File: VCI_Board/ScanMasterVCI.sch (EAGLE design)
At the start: 74 parts, among them IC1 XMEGA16A4A, IC2 CD4081B, IC4 SN74AHCT1G04, IC6 TL331, IC7 74AHCT1G32DBV, IC8 SN74AHCT1G04, Q1 MMBT3904, Q2 MMBT4403LT1SMD, Q3 MMBT4403, Q4 MMBT3904, Q6 NC7SZ18, Q7 ZXMP6A17G, Q9 NC7SZ18, U1 MAX17502FATB+, U2 SN65HVDA195-Q1, U3 MAX17502EATB+, U4 MAX13444EASA+

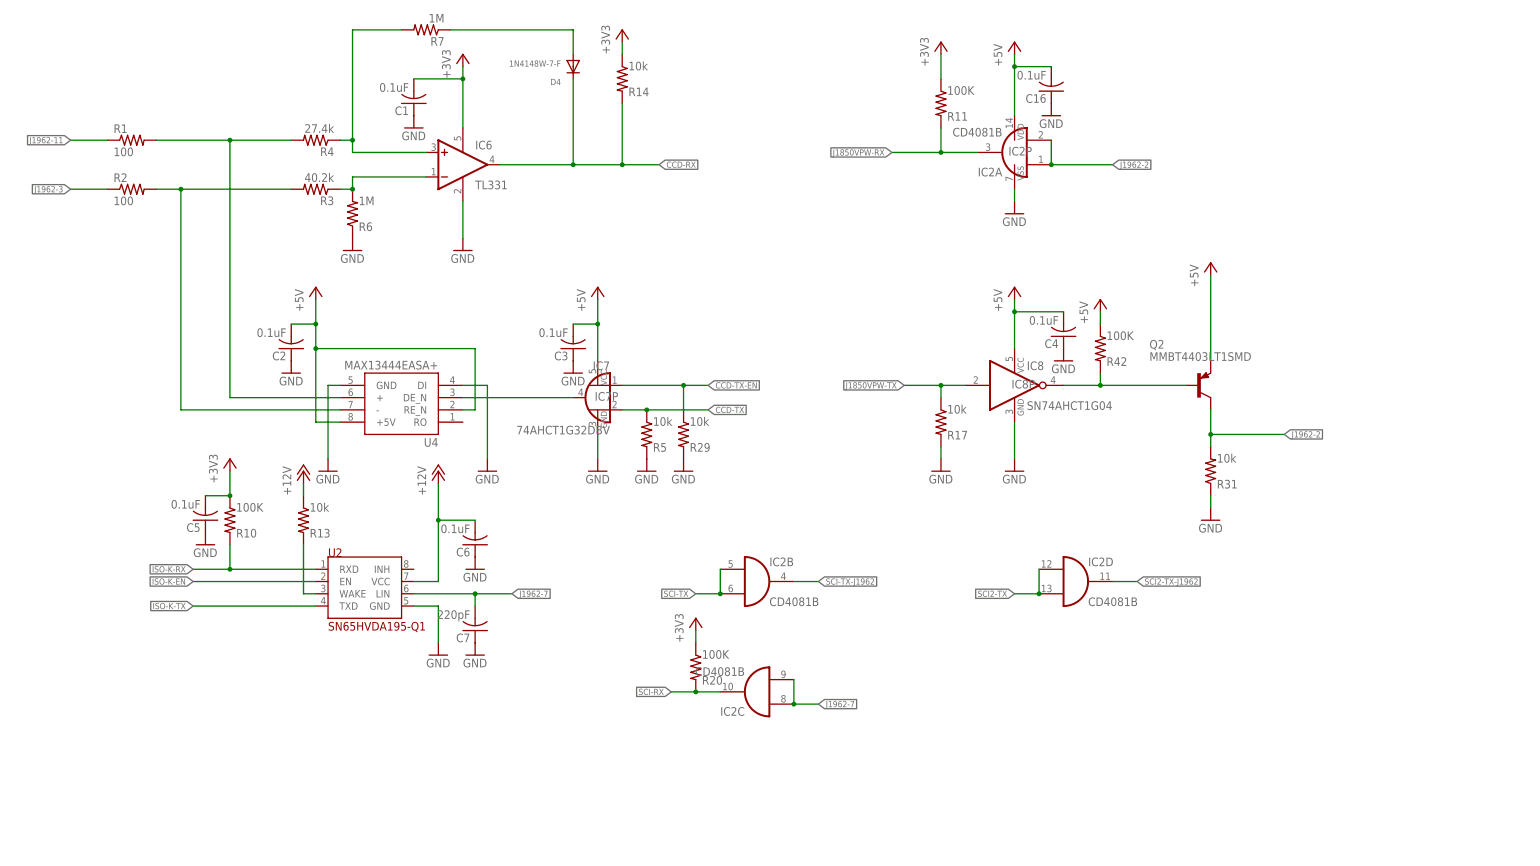
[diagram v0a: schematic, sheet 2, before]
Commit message: Re-did SCI, added activatable ISO9141 pull-up resistor. Based on what I've learned of SCI and how the ECU wiring is done, I've removed all the level shifting from 5V->3.3V, because the bus can be driven in either voltage. I've hooked up the ISO9141 enable pins to transistors that activate pull-up resistors to +12v.
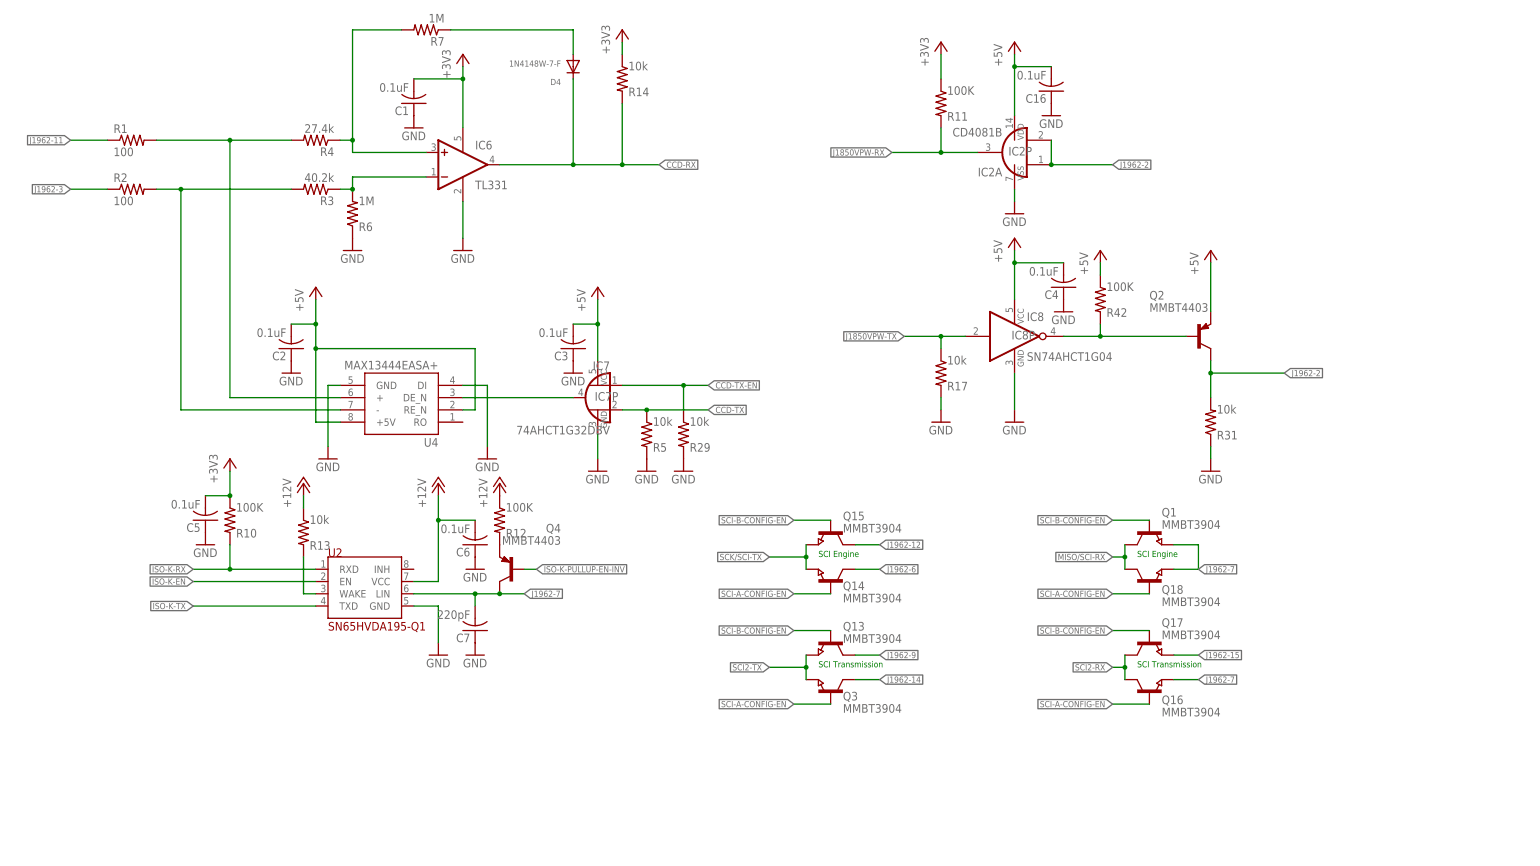
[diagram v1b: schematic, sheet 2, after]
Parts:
- removed C20: 0.1uF, adafruit:C-USC0805
- removed IC4: SN74AHCT1G04, 74xx-little-us:74AHC1G04DBV
- removed Q6, Q9: NC7SZ18, customics:NC7SZ18
- removed R19, R20, R21: 100K, adafruit:R-US_R0805W
- added Q13, Q14, Q15, Q16, Q17, Q18: MMBT3904, semicon-smd-ipc:NPN-TRANSISTOR_SOT23
- added R12: 100K, adafruit:R-US_R0805W
- Q2: value MMBT4403LT1SMD -> MMBT4403
- Q3: value MMBT4403 -> MMBT3904; device transistor-pnp:MMBT4403LT1SMD -> semicon-smd-ipc:NPN-TRANSISTOR_SOT23
- Q4: value MMBT3904 -> MMBT4403; device semicon-smd-ipc:NPN-TRANSISTOR_SOT23 -> transistor-pnp:MMBT4403LT1SMD
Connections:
- removed net J1962-15-5VPULLUP-EN: IC1.PB1, IC4A.I, Q1.B
- removed net J1962-7-5VPULLUP-EN: Q4.B
- removed net MISO: ICSP.1
- removed net N$21: Q4.E, R21.2
- removed net N$25: Q1.E, R19.2
- removed net SCI-RX: IC1.PE2, IC2C.O, R20.2
- removed net SCI-TX: IC2B.I0, IC2B.I1
- removed net SCI-TX-J1962: IC2B.O, Q9.A
- removed net SCI2-TX-J1962: IC2D.O, Q6.A
- removed net SCK: ICSP.3
- new net ISO-K-PULLUP-EN-INV: IC1.PB2, Q4.B
- new net SCI-A-CONFIG-EN: IC1.PB0, Q14.B, Q16.B, Q18.B, Q3.B
- new net SCI2-RX: IC1.PE2, Q16.C, Q17.C
- net +12V: now also R12.1
- net +3V3: no longer R20.1
- net +5V: no longer C20.2, IC4P.VCC, Q6.VCC, Q9.VCC, R19.1, R21.1
- net GND: no longer C20.1, IC4P.GND, Q6.GND, Q9.GND
- net ISO-K-EN: now also IC1.PB3; no longer IC1.PB2
- net J1962-12: now also Q15.C; no longer Q9.Y1
- net J1962-14: now also Q3.C; no longer Q6.Y0
- net J1962-15: now also Q17.E; no longer Q1.C, Q3.E
- net J1962-6: now also Q14.C; no longer Q9.Y0
- net J1962-7: now also Q1.E, Q16.E, Q18.E; no longer IC2C.I0, IC2C.I1, Q3.C
- net J1962-9: now also Q13.C; no longer Q6.Y1
- net MISO/SCI-RX: now also ICSP.1, Q1.C, Q18.C
- net N$10: now also Q4.E, R12.2; no longer IC4A.O, Q3.B
- net SCI-B-CONFIG-EN: now also IC1.PB1, Q1.B, Q13.B, Q15.B, Q17.B; no longer IC1.PB0, Q6.S, Q9.S
- net SCI2-TX: now also Q13.E, Q3.E; no longer IC2D.I0, IC2D.I1
- net SCK/SCI-TX: now also ICSP.3, Q14.E, Q15.E
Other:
- note removed: "Pull-up for Engine/Trans RX on A-Config, Engine only on B-Config"
- note removed: "Pull-up for SCI Trans RX on B-Config"
- note removed: "When activated, if pin 15 pulls low, it will pull 7 low as well."
- moved on the sheet: C4, IC8, IC8P, ICSP, J1962_1, J1962_2, Q2, R13, R17, R31, R42, SERIAL

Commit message: Rewrote CCD circuit, simplified SCI circuit. CCD now relies on an ISO1050 chip to function, based on suggestions. SCI now has a single UART in the XMEGA. This will simplify the design, simultaneous diagnosis of the ECM and TCM is too small a use case to support.
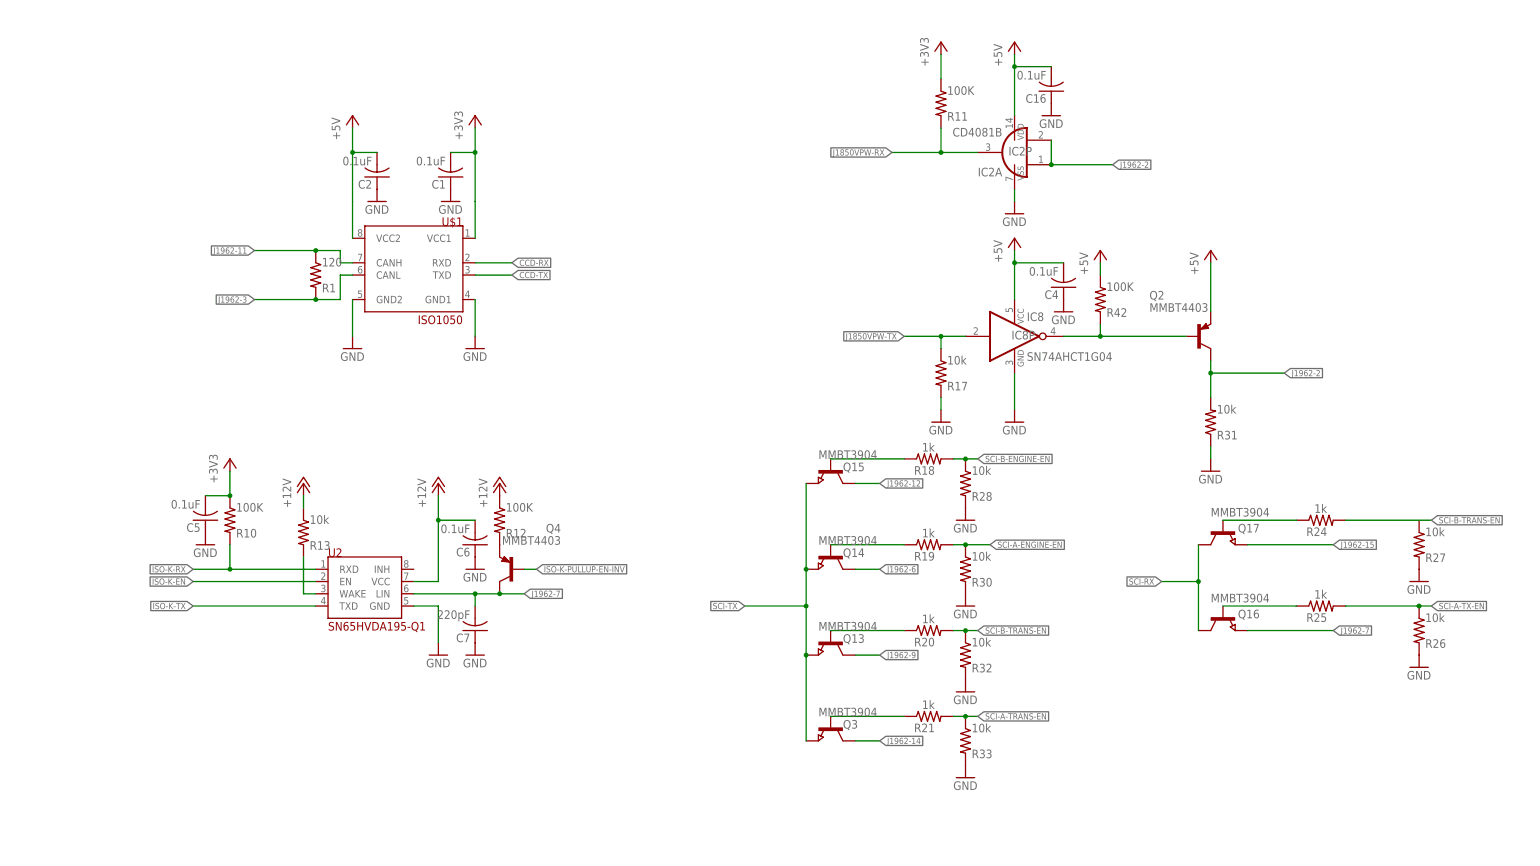
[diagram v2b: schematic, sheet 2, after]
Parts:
- removed C3: 0.1uF, adafruit:C-USC0805
- removed D4: 1N4148W-7-F, customics:1N4148W-7-F
- removed IC6: TL331, linear:TL331
- removed IC7: 74AHCT1G32DBV, 74xx-little-de:74AHCT1G32DBV
- removed Q1, Q18: MMBT3904, semicon-smd-ipc:NPN-TRANSISTOR_SOT23
- removed R14, R29, R5: 10k, adafruit:R-US_R0805
- removed R2: 100, adafruit:R-US_R0805
- removed R3: 40.2k, adafruit:R-US_R0805
- removed R4: 27.4k, adafruit:R-US_R0805
- removed R6, R7: 1M, adafruit:R-US_R0805
- removed U4: MAX13444EASA+, customics:MAX13444EASA+SMD
- added R18, R19, R20, R21, R24, R25: 1k, adafruit:R-US_R0805
- added R26, R27, R28, R30, R32, R33: 10k, adafruit:R-US_R0805
- added U$1: ISO1050, customics:ISO1050
- R1: value 100 -> 120; device adafruit:R-US_R0805 -> adafruit:R-US_R0805W
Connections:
- net SCI2-RX renamed SCI-RX
- removed net CCD-TX-EN: IC7A.I0, R29.1
- removed net MISO/SCI-RX: IC1.PC6, ICSP.1, Q1.C, Q18.C
- removed net N$11: R1.2, R4.2, U4.+
- removed net N$2: IC6.-IN, R3.1, R6.2
- removed net N$3: D4.A, R7.1
- removed net N$6: IC7A.O, U4.DE_N
- removed net SCI-A-CONFIG-EN: IC1.PB0, Q14.B, Q16.B, Q18.B, Q3.B
- removed net SCI-B-CONFIG-EN: IC1.PB1, Q1.B, Q13.B, Q15.B, Q17.B
- removed net SCI2-TX: IC1.PE3, Q13.E, Q3.E
- removed net SCK/SCI-TX: IC1.PC7, ICSP.3, Q14.E, Q15.E
- new net MISO: IC1.PC6, ICSP.1
- new net N$13: Q15.B, R18.1
- new net N$21: Q14.B, R19.1
- new net N$22: Q13.B, R20.1
- new net N$23: Q3.B, R21.1
- new net N$24: Q17.B, R24.1
- new net N$25: Q16.B, R25.1
- new net SCI-A-ENGINE-EN: IC1.PB0, R19.2, R30.1
- new net SCI-A-TRANS-EN: IC1.PB2, R21.2, R33.1
- new net SCI-A-TX-EN: IC1.PE0, R25.2, R26.1
- new net SCI-B-ENGINE-EN: IC1.PB1, R18.2, R28.1
- new net SCI-B-TRANS-EN: IC1.PB3, R20.2, R24.2, R32.1
- new net SCI-TX: IC1.PE3, Q13.E, Q14.E, Q15.E, Q3.E
- new net SCK: IC1.PC7, ICSP.3
- net +3V3: no longer IC6.V+, R14.1
- net +5V: no longer C3.2, IC7P.VCC, U4.+5V, U4.RE_N
- net CCD-RX: now also U$1.RXD; no longer D4.C, IC6.OUT, R14.2
- net CCD-TX: now also U$1.TXD; no longer IC7A.I1, R5.1
- net GND: now also R26.2, R27.2, R28.2, R30.2, R32.2, R33.2, U$1.GND1, U$1.GND2; no longer C3.1, IC6.GND, IC7P.GND, R29.2, R5.2, R6.1, U4.DI, U4.GND
- net ISO-K-EN: now also IC1.PD5; no longer IC1.PB3
- net ISO-K-PULLUP-EN-INV: now also IC1.PD4; no longer IC1.PB2
- net J1962-11: now also U$1.CANH
- net J1962-3: now also R1.2, U$1.CANL; no longer R2.1
- net J1962-7: no longer Q1.E, Q18.E
- net N$1: now also U$1.VCC2; no longer IC6.+IN, R4.1, R7.2
- net N$4: now also U$1.VCC1; no longer R2.2, R3.2, U4.-
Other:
- note removed: "SCI Transmission"
- moved on the sheet: C1, C2, Q14, Q15, Q16, Q17, Q3, R1

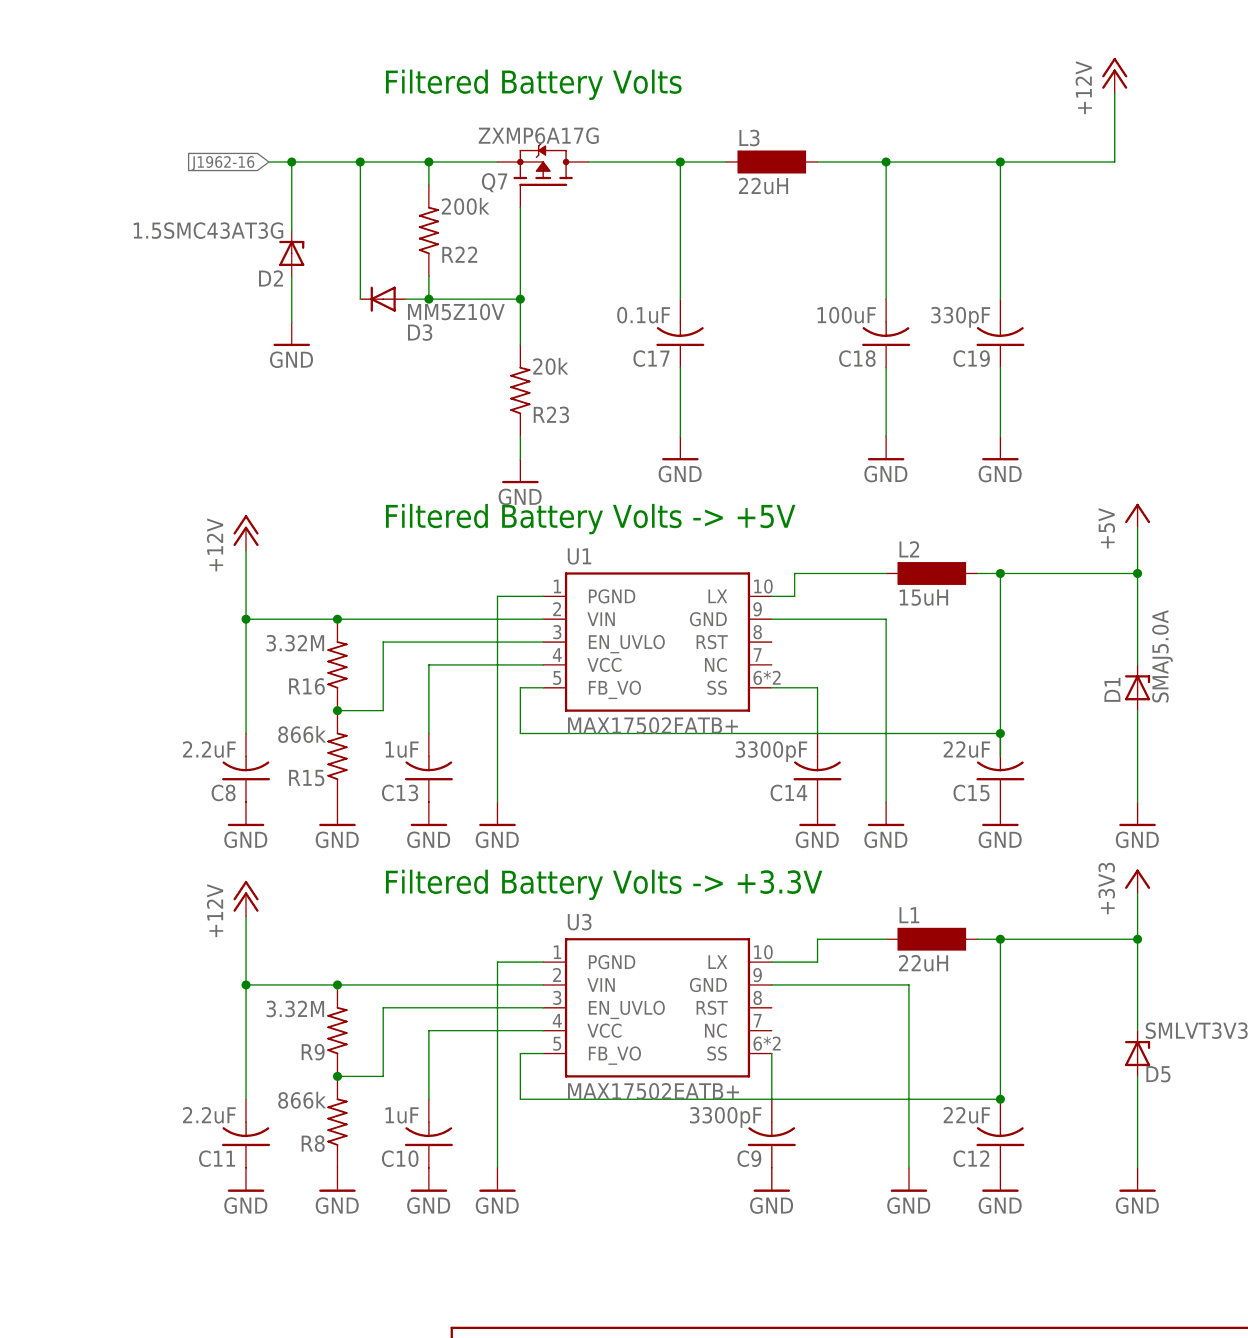
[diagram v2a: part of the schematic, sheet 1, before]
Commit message: Capacitors had reversed polarity. Corrected.
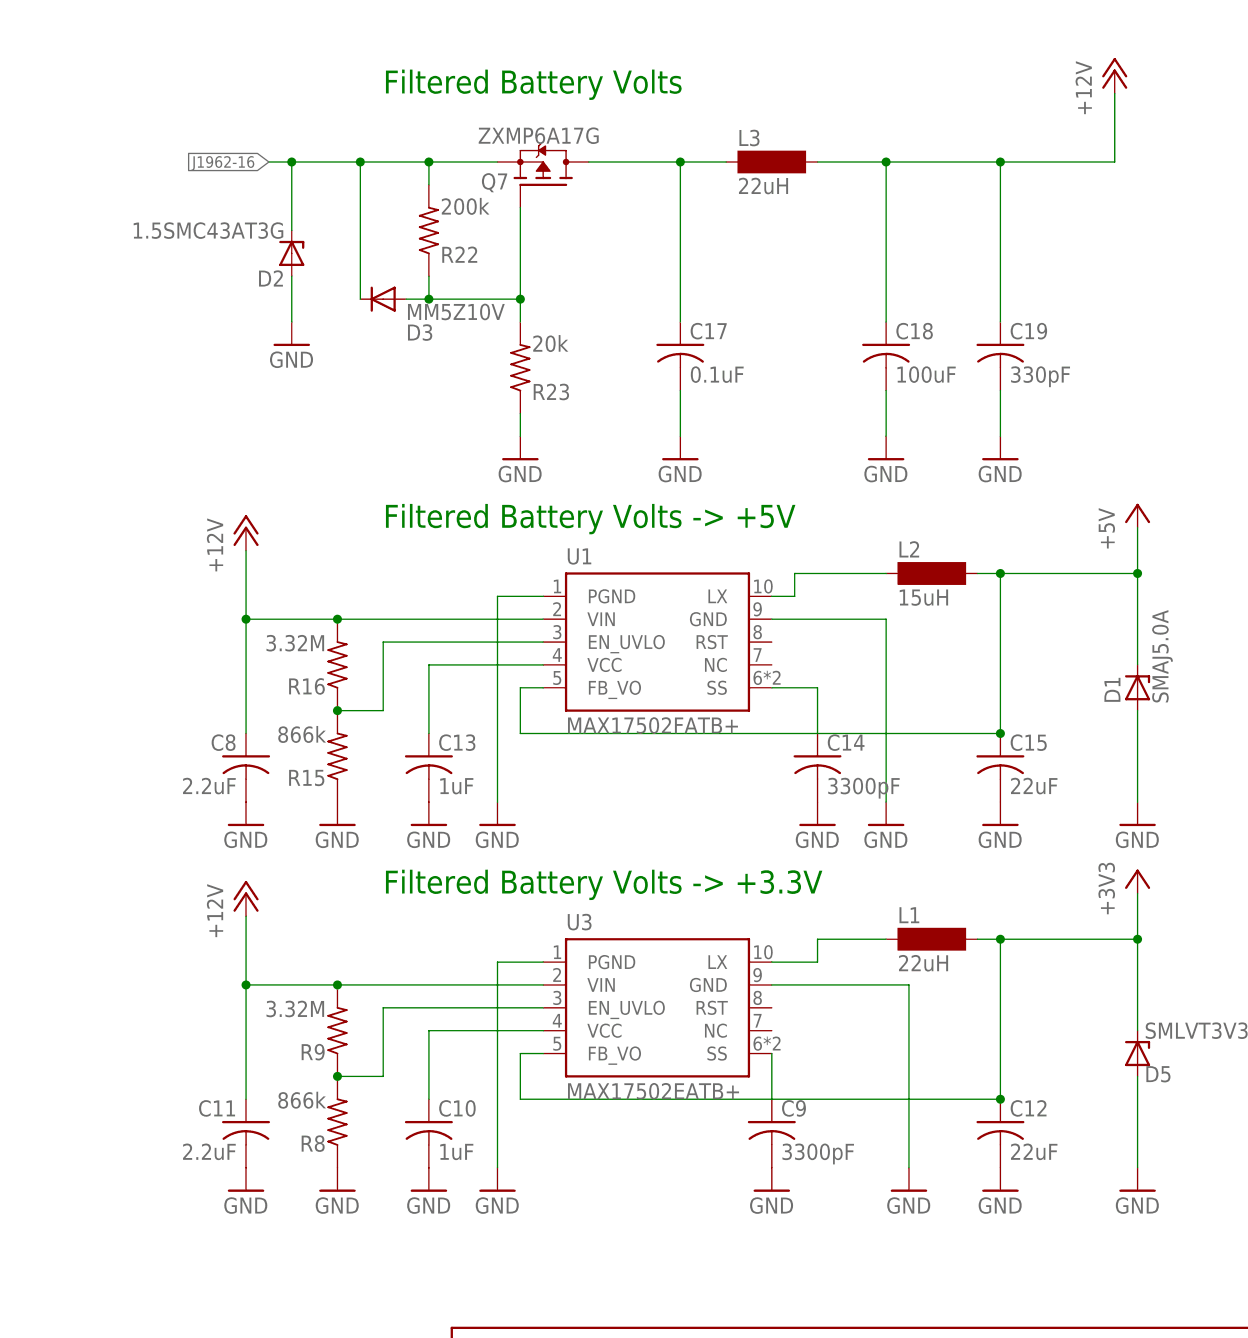
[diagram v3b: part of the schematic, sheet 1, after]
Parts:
- removed C16: 0.1uF, adafruit:C-USC0805
- added C3: 0.1uF, adafruit:C-USC0805
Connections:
- removed net N$8: C9.2, U3.SS
- new net N$3: C9.1, U3.SS
- net +12V: now also C11.1, C18.1, C19.1, C3.1, C8.1; no longer C11.2, C18.2, C19.2, C6.2, C8.2
- net +3V3: now also C12.1, C2.1, C5.1; no longer C1.2, C12.2, C5.2
- net +5V: now also C1.1, C15.1, C4.1, C6.1; no longer C15.2, C16.2, C2.2, C4.2
- net GND: now also C1.2, C10.2, C11.2, C12.2, C13.2, C14.2, C15.2, C17.2, C18.2, C19.2, C2.2, C3.2, C4.2, C5.2, C6.2, C7.2, C8.2, C9.2; no longer C1.1, C10.1, C11.1, C12.1, C13.1, C14.1, C15.1, C16.1, C17.1, C18.1, C19.1, C2.1, C4.1, C5.1, C6.1, C7.1, C8.1, C9.1
- net J1962-7: now also C7.1; no longer C7.2
- net N$15: now also C13.1; no longer C13.2
- net N$17: now also C14.1; no longer C14.2
- net N$18: now also C17.1; no longer C17.2
- net N$9: now also C10.1; no longer C10.2
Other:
- moved on the sheet: C1, C10, C11, C12, C13, C14, C15, C17, C18, C19, C2, C4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
